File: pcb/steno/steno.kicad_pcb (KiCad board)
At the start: 2 copper layers, 259.5 x 85.1 mm, 61 parts, among them J1 USB_C_Receptacle_USB2.0, K1 PG1350, K10 PG1350, K11 PG1350, K12 PG1350, K13 PG1350, K14 PG1350, K15 PG1350, K16 PG1350, K17 PG1350, K18 PG1350, K19 PG1350, K2 PG1350, K20 PG1350, K21 PG1350, K22 PG1350, K23 PG1350, K24 PG1350, K25 PG1350, K26 PG1350, K27 PG1350, K28 PG1350, K29 PG1350, K3 PG1350, K30 PG1350, K4 PG1350, K5 PG1350, K6 PG1350, K7 PG1350, K8 PG1350, K9 PG1350, SW1 SW_Push, SW2 SW_Push, U1 ATmega32U4-AU, U2 MT25QL128ABA1ESE, U3 MCP1700-3302E_SOT23, U4 LCD2.2in, U5 4050, U6 SRV05-4, Y1 16MHz

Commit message: [pcb] 2 row Auklet
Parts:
- removed C10, C9: 1uF, Capacitor_SMD:C_0805_2012Metric
- removed C5, C6, C7: 104, Capacitor_SMD:C_0603_1608Metric
- removed C8: 10uF, Capacitor_SMD:C_0805_2012Metric
- removed F1: Polyfuse_Small, Fuse:Fuse_1206_3216Metric_Castellated
- removed Y1: 16MHz, Crystal:Crystal_SMD_EuroQuartz_MT-4Pin_3.2x2.5mm
- added BT1: Battery_Cell, Connector_JST:JST_PH_S2B-PH-SM4-TB_1x02-1MP_P2.00mm_Horizontal, F.Cu at (156.6, 67.7)
- added D1: RED, LED_SMD:LED_0805_2012Metric, F.Cu at (146.9, 54.7)
- added D2: LED_RABG, LED_SMD:LED_ASMB-KTF0-0A306, F.Cu at (135.4, 65.5)
- added H1: MountingHole, misc:auklet-mount, F.Cu at (138.9, 100.7)
- added H2: MountingHole, misc:auklet-cover-mount, F.Cu at (138.9, 100.7)
- added J2: USB_C_Receptacle_USB2.0, Connector_USB:USB_C_Receptacle_HRO_TYPE-C-31-M-12, F.Cu at (138.9, 56.9)
- added Q1: AO3401A, Package_TO_SOT_SMD:SOT-23, F.Cu at (144.9, 76.2)
- added R1: 100k, Resistor_SMD:R_0603_1608Metric, F.Cu at (114.4, 78.7)
- added R13: 5.1M, Resistor_SMD:R_0603_1608Metric, F.Cu at (134.4, 69.7)
- added R14: 5.1M, Resistor_SMD:R_0603_1608Metric, F.Cu at (133.6, 67.5)
- added R15: 1.2k, Resistor_SMD:R_0603_1608Metric, F.Cu at (132.1, 59.2)
- added R16: 1.5k, Resistor_SMD:R_0603_1608Metric, F.Cu at (132.1, 65.0)
- added R17: 1k, Resistor_SMD:R_0603_1608Metric, F.Cu at (132.6, 62.7)
- added R6: 220, Resistor_SMD:R_0603_1608Metric, F.Cu at (116.6, 112.2)
- added REF**: crides-neg, misc:crides-neg, F.Cu at (87.4, 102.7)
- added REF**: embedded, misc:embedded, F.Cu at (99.9, 105.2)
- C1, C2: value 22pF -> 4.7uF; moved to F.Cu
- C3: value 1uF -> 4.7uF; footprint Capacitor_SMD:C_0805_2012Metric -> Capacitor_SMD:C_0603_1608Metric; moved to F.Cu
- C4: value 1uF -> 10nF; footprint Capacitor_SMD:C_0805_2012Metric -> Capacitor_SMD:C_0603_1608Metric; moved to F.Cu
- J1: value USB_C_Receptacle_USB2.0 -> Conn_01x04; footprint Connector_USB:USB_C_Receptacle_HRO_TYPE-C-31-M-12 -> keeb-libs:debug-port-single-side
- K1, K10, K11, K12, K13, K14, K15, K16, K17, K18, K19, K2, K20, K21, K22, K23, K24, K25, K26, K27, K28, K29, K3, K30, K4, K5, K6, K7, K8, K9: value PG1350 -> diode-choc; footprint pg1350:PG1350 -> pg1350:pg1350-D
- R10: value 220 -> 10k; moved to F.Cu
- R11: value 5.1k -> 10k; moved to F.Cu
- R12: value 5.1k -> 1k; moved to F.Cu
- R2, R3: value 22 -> 220; moved to F.Cu
- R4: value 10k -> 100; footprint Resistor_SMD:R_0805_2012Metric -> Resistor_SMD:R_0603_1608Metric; moved to F.Cu
- R5: value 10k -> 220; footprint Resistor_SMD:R_0805_2012Metric -> Resistor_SMD:R_0603_1608Metric; moved to F.Cu
- R7: value 220 -> 100k; moved to F.Cu
- R8, R9: value 220 -> 5.1k; moved to F.Cu
- SW1: value SW_Push -> SW_SPDT; footprint Button_Switch_SMD:SW_SPST_B3U-1000P -> Button_Switch_SMD:SW_SPDT_PCM12
- SW2: footprint Button_Switch_SMD:SW_SPST_B3U-1000P -> Button_Switch_SMD:SW_SPST_TL3342
- U1: value ATmega32U4-AU -> MT25QL128ABA1ESE; footprint Package_QFP:TQFP-44_10x10mm_P0.8mm -> Package_SO:SOP-8_5.28x5.23mm_P1.27mm; moved to F.Cu
- U2: value MT25QL128ABA1ESE -> LCD2.2in; footprint Package_SO:SOP-8_5.28x5.23mm_P1.27mm -> misc:TM022HDH26; moved to F.Cu
- U3: value MCP1700-3302E_SOT23 -> Holyiot_18010_no_underside; footprint Package_TO_SOT_SMD:SOT-23 -> keeb-libs:Holyiot-18010-no-underside; moved to F.Cu
- U4: value LCD2.2in -> BQ24075; footprint steno:LCD2.2in -> Package_DFN_QFN:VQFN-16-1EP_3x3mm_P0.5mm_EP1.68x1.68mm_ThermalVias
- U5: value 4050 -> XC6206B331MR; footprint Package_SO:SOIC-16_3.9x9.9mm_P1.27mm -> Package_TO_SOT_SMD:SOT-23-5; moved to F.Cu
- U6: moved to F.Cu
- moved R9 52.9 mm to (132.1, 57.7)
- moved R8 52.0 mm to (145.1, 57.2), turned to -90 degrees
- moved R3 45.8 mm to (116.6, 109.2), turned to 180 degrees
- moved R2 45.2 mm to (116.6, 107.7), turned to 180 degrees
- moved R7 37.6 mm to (146.9, 73.0), turned to 90 degrees
- moved U5 36.4 mm to (148.6, 67.2)
- moved R10 35.7 mm to (143.1, 71.0), turned to -90 degrees
- moved J1 31.8 mm to (108.6, 56.7), turned to 15 degrees
- moved R5 25.7 mm to (116.6, 110.7), turned to 180 degrees
- moved U4 25.5 mm to (144.6, 67.2), turned to 90 degrees
- moved U1 24.9 mm to (118.4, 75.0), turned to 180 degrees
- moved C1 21.7 mm to (142.4, 64.0)
- moved U3 20.2 mm to (122.9, 61.9)
- moved R4 17.2 mm to (144.6, 73.7)
- moved SW2 16.0 mm to (133.6, 74.2), turned to 0 degrees
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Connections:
- C1 pad 1: Net-(C1-Pad1) -> VBUS
- C2 pad 1: Net-(C2-Pad1) -> GND
- C2 pad 2: GND -> /power/VDDH
- C3 pad 1: GND -> /power/BAT
- C3 pad 2: Net-(C3-Pad2) -> GND
- C4 pad 1: Net-(C4-Pad1) -> BAT_MEAS
- K1 pad 1: ROW1 -> R1
- K1 pad 2: COL1 -> C1
- K1 pad 3: Net-(K1-Pad3) -> (no net)
- K10 pad 1: ROW2 -> R2
- K10 pad 2: COL4 -> C4
- K10 pad 3: Net-(K10-Pad3) -> (no net)
- K11 pad 1: ROW2 -> R2
- K11 pad 2: COL5 -> C5
- K11 pad 3: Net-(K11-Pad3) -> (no net)
- K12 pad 1: ROW2 -> R2
- K12 pad 2: COL6 -> C6
- K12 pad 3: Net-(K12-Pad3) -> (no net)
- K13 pad 1: ROW3 -> R3
- K13 pad 2: COL1 -> C1
- K13 pad 3: Net-(K13-Pad3) -> (no net)
- K14 pad 1: ROW3 -> R3
- K14 pad 2: COL2 -> C2
- K14 pad 3: Net-(K14-Pad3) -> (no net)
- K15 pad 1: ROW3 -> R3
- K15 pad 2: COL3 -> C3
- K15 pad 3: Net-(K15-Pad3) -> (no net)
- K16 pad 1: ROW3 -> R3
- K16 pad 2: COL4 -> C4
- K16 pad 3: Net-(K16-Pad3) -> (no net)
- K17 pad 1: ROW3 -> R3
- K17 pad 2: COL5 -> C5
- K17 pad 3: Net-(K17-Pad3) -> (no net)
- K18 pad 1: ROW3 -> R3
- K18 pad 2: COL6 -> C6
- K18 pad 3: Net-(K18-Pad3) -> (no net)
- K19 pad 1: ROW4 -> R4
- K19 pad 2: COL1 -> C1
- K19 pad 3: Net-(K19-Pad3) -> (no net)
- K2 pad 1: ROW1 -> R1
- K2 pad 2: COL2 -> C2
- K2 pad 3: Net-(K2-Pad3) -> (no net)
- K20 pad 1: ROW4 -> R4
- K20 pad 2: COL2 -> C2
- K20 pad 3: Net-(K20-Pad3) -> (no net)
- K21 pad 1: ROW4 -> R4
- K21 pad 2: COL3 -> C3
- K21 pad 3: Net-(K21-Pad3) -> (no net)
- K22 pad 1: ROW4 -> R4
- K22 pad 2: COL4 -> C4
- K22 pad 3: Net-(K22-Pad3) -> (no net)
- K23 pad 1: ROW4 -> R4
- K23 pad 2: COL5 -> C5
- K23 pad 3: Net-(K23-Pad3) -> (no net)
- K24 pad 1: ROW4 -> R4
- K24 pad 2: COL6 -> C6
- K24 pad 3: Net-(K24-Pad3) -> (no net)
- K25 pad 1: ROW5 -> R5
- K25 pad 2: COL1 -> C1
- K25 pad 3: Net-(K25-Pad3) -> (no net)
- K26 pad 1: ROW5 -> R5
- K26 pad 2: COL2 -> C2
- K26 pad 3: Net-(K26-Pad3) -> (no net)
- K27 pad 1: ROW5 -> R5
- K27 pad 2: COL3 -> C3
- K27 pad 3: Net-(K27-Pad3) -> (no net)
- K28 pad 1: ROW5 -> R5
- K28 pad 2: COL4 -> C4
- K28 pad 3: Net-(K28-Pad3) -> (no net)
- K29 pad 1: ROW5 -> R5
- K29 pad 2: COL5 -> C5
- K29 pad 3: Net-(K29-Pad3) -> (no net)
- K3 pad 1: ROW1 -> R1
- K3 pad 2: COL3 -> C3
- K3 pad 3: Net-(K3-Pad3) -> (no net)
- K30 pad 1: ROW5 -> R5
- K30 pad 2: COL6 -> C6
- K30 pad 3: Net-(K30-Pad3) -> (no net)
- K4 pad 1: ROW1 -> R1
- K4 pad 2: COL4 -> C4
- K4 pad 3: Net-(K4-Pad3) -> (no net)
- K5 pad 1: ROW1 -> R1
- K5 pad 2: COL5 -> C5
- K5 pad 3: Net-(K5-Pad3) -> (no net)
- K6 pad 1: ROW1 -> R1
- K6 pad 2: COL6 -> C6
- K6 pad 3: Net-(K6-Pad3) -> (no net)
- K7 pad 1: ROW2 -> R2
- K7 pad 2: COL1 -> C1
- K7 pad 3: Net-(K7-Pad3) -> (no net)
- K8 pad 1: ROW2 -> R2
- K8 pad 2: COL2 -> C2
- K8 pad 3: Net-(K8-Pad3) -> (no net)
- K9 pad 1: ROW2 -> R2
- K9 pad 2: COL3 -> C3
- K9 pad 3: Net-(K9-Pad3) -> (no net)
- R11 pad 1: GND -> Net-(R11-Pad1)
- R11 pad 2: Net-(J1-PadA5) -> GND
- R12 pad 1: GND -> Net-(R12-Pad1)
- R12 pad 2: Net-(J1-PadB5) -> Net-(D1-Pad1)
- R2 pad 2: D+ -> GND
- R3 pad 2: D- -> GND
- R4 pad 1: GND -> BL
- R4 pad 2: Net-(R4-Pad2) -> Net-(Q1-Pad1)
- R5 pad 2: +3V3 -> GND
- R7 pad 1: Net-(R7-Pad1) -> Net-(Q1-Pad1)
- R8 pad 1: Net-(R8-Pad1) -> GND
- R8 pad 2: GND -> Net-(J2-PadA5)
- R9 pad 1: Net-(R9-Pad1) -> GND
- R9 pad 2: GND -> Net-(J2-PadB5)
- SW1 pad 1: GND -> VBUS
- SW1 pad 2: RESET -> Net-(SW1-Pad2)
- U1 pad 1: Net-(U1-Pad1) -> FLASH_CS
- U1 pad 2: +5V -> MISO
- U1 pad 3: Net-(R3-Pad1) -> DQ2
- U1 pad 4: Net-(R2-Pad1) -> GND
- U1 pad 5: GND -> MOSI
- U1 pad 6: Net-(C4-Pad1) -> SCLK
- U1 pad 7: +5V -> DQ2
- U1 pad 8: Net-(SW2-Pad2) -> +3V3
- U2 pad 1: CS_3V3 -> GND
- U2 pad 2: MISO -> +3V3
- U2 pad 3: Net-(R5-Pad1) -> SCLK
- U2 pad 4: GND -> C\D
- U2 pad 5: MOSI_3V3 -> LCD_CS
- U2 pad 6: SCLK_3V3 -> MOSI
- U2 pad 7: Net-(R5-Pad1) -> MISO
- U2 pad 8: +3V3 -> GND
- U3 pad 2: +3V3 -> unconnected-(U3-Pad2)
- U3 pad 3: +5V -> unconnected-(U3-Pad3)
- U4 pad 1: GND -> Net-(R10-Pad1)
- U4 pad 10: +3V3 -> /power/VDDH
- U4 pad 11: Net-(R7-Pad1) -> /power/VDDH
- U4 pad 12: Net-(R8-Pad1) -> unconnected-(U4-Pad12)
- U4 pad 13: Net-(R9-Pad1) -> VBUS
- U4 pad 14: Net-(R10-Pad1) -> unconnected-(U4-Pad14)
- U4 pad 2: +3V3 -> /power/BAT
- U4 pad 3: SCLK_3V3 -> /power/BAT
- U4 pad 4: C\D_3V3 -> GND
- U4 pad 5: LCD_CS_3V3 -> GND
- U4 pad 6: MOSI_3V3 -> /power/VDDH
- U4 pad 7: MISO -> unconnected-(U4-Pad7)
- U4 pad 9: +3V3 -> Net-(R12-Pad1)
- U5 pad 1: +3V3 -> /power/VDDH
- U5 pad 2: SCLK_3V3 -> GND
- U5 pad 3: SCLK_5V -> Net-(SW1-Pad2)
- U5 pad 4: MOSI_3V3 -> unconnected-(U5-Pad4)
- U5 pad 5: MOSI_5V -> +3V3
- U6 pad 1: Net-(U6-Pad1) -> D+
- U6 pad 3: Net-(U6-Pad3) -> D-
- U6 pad 4: D+ -> D-
- U6 pad 5: VCC -> VBUS
- U6 pad 6: D- -> D+
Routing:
- net C1: track 0.00 -> 358.0 mm, vias 0 -> 3
- net COL1: track 329.7 -> 0.00 mm, vias 1 -> 0
- net C2: track 0.00 -> 322.3 mm, vias 0 -> 5
- net COL2: track 292.9 -> 0.00 mm, vias 3 -> 0
- net C3: track 0.00 -> 290.5 mm, vias 0 -> 5
- net COL3: track 260.4 -> 0.00 mm, vias 3 -> 0
- net C4: track 0.00 -> 256.3 mm, vias 0 -> 5
- net COL4: track 224.5 -> 0.00 mm, vias 3 -> 0
- net C5: track 0.00 -> 218.3 mm, vias 0 -> 5
- net R3: track 0.00 -> 190.4 mm, vias 0 -> 2
- net COL5: track 184.8 -> 0.00 mm, vias 3 -> 0
- net C6: track 0.00 -> 178.0 mm, vias 0 -> 5
- net ROW3: track 161.7 -> 0.00 mm
- net COL6: track 148.9 -> 0.00 mm, vias 3 -> 0
- net R5: track 0.00 -> 146.2 mm, vias 0 -> 1
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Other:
- board size 259.5 x 85.1 mm -> 268.1 x 85.4 mm
- net class Default removed
- board text added: "Auklet (embedded steno board v4) Open sourced @ github.com/crides/steno"
- board text added: "No"
- board text added: "Use Bat"
- board text added: "Yes"
- board text removed: "BatWings Embedded steno gives you wings!"
- board text removed: "Open sourced @ github.com/crides/steno"
- board text removed: "Public test #1"

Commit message: [pcb] Auklet 3
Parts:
- added K32: diode-choc, pg1350:pg1350-D, F.Cu at (36.2, 103.5)
- added K33: diode-choc, pg1350:pg1350-D, F.Cu at (54.8, 101.7)
- added K34: diode-choc, pg1350:pg1350-D, F.Cu at (73.1, 101.9)
- added K35: diode-choc, pg1350:pg1350-D, F.Cu at (90.3, 108.0)
- added K36: diode-choc, pg1350:pg1350-D, F.Cu at (108.0, 111.1)
- added K38: diode-choc, pg1350:pg1350-D, F.Cu at (259.3, 103.5)
- added K39: diode-choc, pg1350:pg1350-D, F.Cu at (240.7, 101.7)
- added K40: diode-choc, pg1350:pg1350-D, F.Cu at (222.5, 101.9)
- added K41: diode-choc, pg1350:pg1350-D, F.Cu at (205.3, 108.0)
- added K42: diode-choc, pg1350:pg1350-D, F.Cu at (187.6, 111.1)
- moved BT1 114.9 mm to (269.1, 91.1)
- moved REF** 35.3 mm to (65.5, 113.2)
- moved REF** 35.0 mm to (53.3, 110.6)
- moved K30 8.96 mm to (184.6, 94.3)
- moved C3 8.96 mm to (154.5, 69.3)
- moved R13 8.96 mm to (143.3, 68.8)
- moved U5 8.96 mm to (157.5, 66.3)
- moved C1 8.96 mm to (151.3, 63.0)
- moved K8 8.96 mm to (39.2, 86.8)
- moved U2 8.96 mm to (147.8, 104.8)
- moved K14 8.96 mm to (100.6, 127.5)
- moved R9 8.96 mm to (141.0, 56.8)
- moved U6 8.96 mm to (147.8, 64.0)
- moved K4 8.96 mm to (79.0, 68.4)
- moved K9 8.96 mm to (57.8, 85.0)
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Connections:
- K13 pad 1: R3 -> R4
- K14 pad 1: R3 -> R4
- K15 pad 1: R3 -> R4
- K16 pad 1: R3 -> R4
- K17 pad 1: R3 -> R4
- K18 pad 1: R3 -> R4
- K19 pad 1: R4 -> R5
- K20 pad 1: R4 -> R5
- K21 pad 1: R4 -> R5
- K22 pad 1: R4 -> R5
- K23 pad 1: R4 -> R5
- K24 pad 1: R4 -> R5
- K25 pad 1: R5 -> R6
- K26 pad 1: R5 -> R6
- K27 pad 1: R5 -> R6
- K28 pad 1: R5 -> R6
- K29 pad 1: R5 -> R6
- K30 pad 1: R5 -> R6
- U3 pad 41: R4 -> R5
- U3 pad 42: R5 -> R6
- U3 pad 43: R3 -> R4
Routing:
- net R6: track 0.00 -> 146.2 mm, vias 0 -> 1
- net /power/BAT: track 28.2 -> 147.9 mm, vias 3 -> 5
- net R3: track 190.4 -> 76.6 mm, vias 2 -> 0
- net GND: track 131.2 -> 231.2 mm, vias 18 -> 19
- net R7: track 0.00 -> 76.6 mm
- net C3: track 290.5 -> 341.9 mm
- net R4: track 140.0 -> 189.1 mm, vias 1 -> 2
- net C2: track 322.3 -> 371.2 mm
- net C5: track 218.3 -> 266.3 mm
- net C4: track 256.3 -> 304.0 mm
- net C6: track 178.0 -> 213.7 mm
- net C1: track 358.0 -> 393.3 mm
- net R5: track 146.2 -> 140.0 mm
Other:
- board size 268.1 x 85.4 mm -> 268.7 x 85.3 mm
- board text added: "+ -"

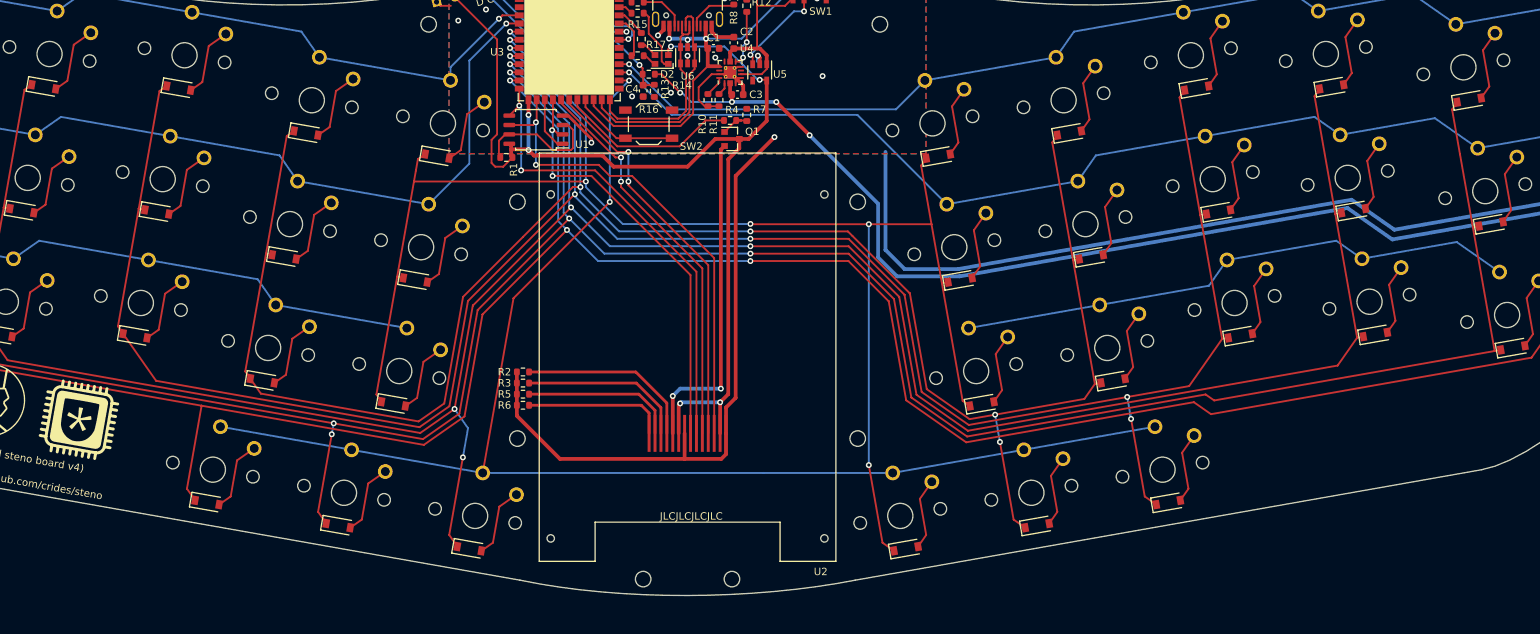
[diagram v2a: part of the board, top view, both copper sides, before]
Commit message: [pcb] auklet 3: use new libraries
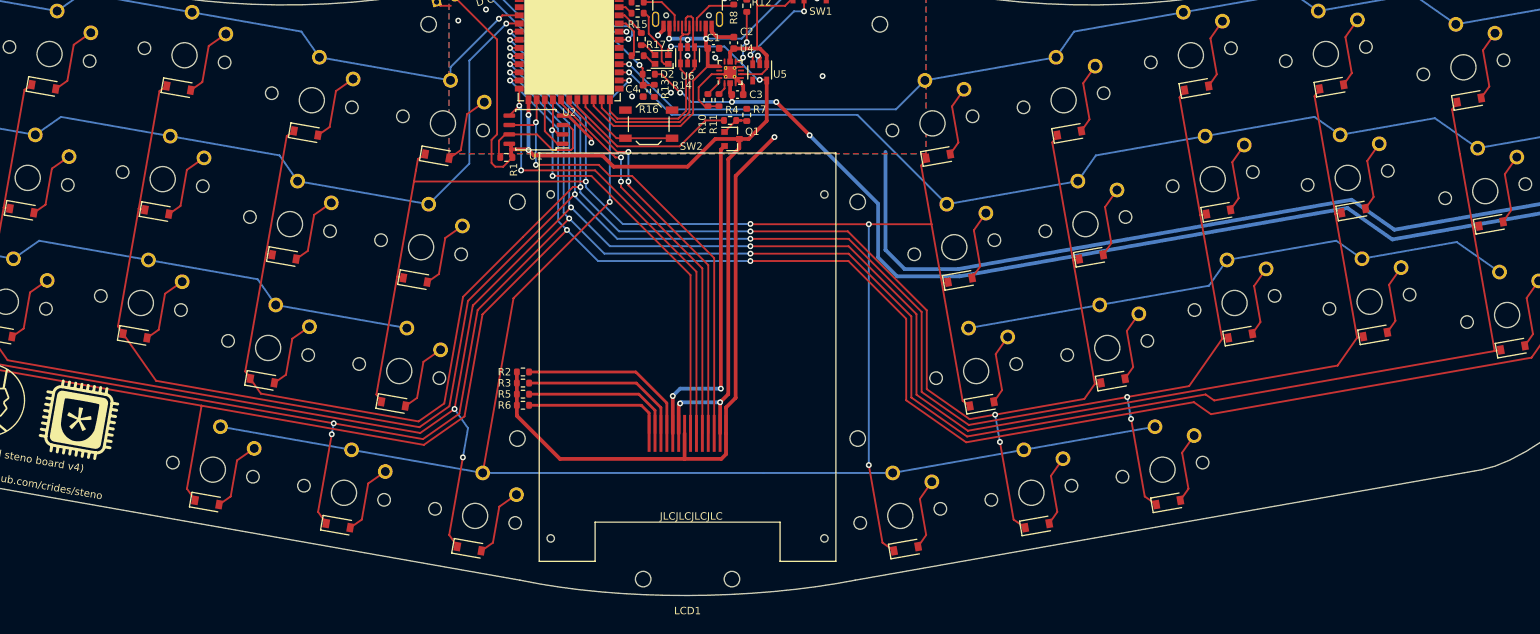
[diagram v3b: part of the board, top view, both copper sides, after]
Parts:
- LCD1: renamed from U2; value LCD2.2in -> TM022HDH26; footprint misc:TM022HDH26 -> display:TM022HDH26
- U1: footprint Package_SO:SOP-8_5.28x5.23mm_P1.27mm -> Package_SO:SOIC-8_5.23x5.23mm_P1.27mm
- U2: renamed from U3; value Holyiot_18010_no_underside -> holyiot-18010-no-underside; footprint keeb-libs:Holyiot-18010-no-underside -> mcu:Holyiot-18010-no-underside
- renumbered K32 to K31, K33 to K32, K34 to K33, K35 to K34, K36 to K35, K38 to K36, K39 to K37, K40 to K38, K41 to K39, K42 to K40
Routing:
- net C1: track 393.3 -> 394.0 mm
- net C3: track 341.9 -> 342.7 mm
- net C2: track 371.2 -> 371.9 mm
- net C4: track 304.0 -> 304.8 mm
- net C5: track 266.3 -> 267.1 mm

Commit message: [pcb] Auklet 3: first revision
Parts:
- J1: value Conn_01x04 -> debug-port; footprint keeb-libs:debug-port-single-side -> misc:debug-port-single-side
- U2: footprint mcu:Holyiot-18010-no-underside -> mcu:holyiot-18010-no-underside
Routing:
- net GND: track 231.2 -> 228.4 mm, vias 19 -> 20
- net Net-(SW1-Pad2): track 12.9 -> 11.3 mm
- net DQ2: track 17.8 -> 17.0 mm
- net Net-(Q1-Pad1): track 4.24 -> 3.57 mm
- net MISO: track 57.4 -> 56.8 mm

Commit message: [pcb] Auklet: add tooling holes
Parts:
- added REF**: jlc-tooling-hole, misc:jlc-tooling-hole, F.Cu at (147.8, 131.0)
- added REF**: jlc-tooling-hole, misc:jlc-tooling-hole, F.Cu at (21.8, 55.3)
- added REF**: jlc-tooling-hole, misc:jlc-tooling-hole, F.Cu at (272.8, 55.3)
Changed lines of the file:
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@@
     )
+  )
+  (footprint "misc:jlc-tooling-hole" (layer "F.Cu")
+    (at 147.775972 131.027909)
+    (attr through_hole board_only exclude_from_pos_files exclude_from_bom)
+    (fp_text reference "REF**" (at 0 -4 unlocked) (layer "F.SilkS") hide
+      (effects (font (size 1 1) (thickness 0.15)))
+    )
+    (fp_text value "jlc-tooling-hole" (at 0 1.5 unlocked) (layer "F.Fab")
+      (effects (font (size 1 1) (thickness 0.15)))
+    )
+    (pad "" np_thru_hole circle (at 0 0) (size 1.3 1.3) (drill 1.152) (layers *.Mask))
   )
   (footprint "misc:auklet-mount" (layer "F.Cu")
@@
     )
   )
+  (footprint "misc:jlc-tooling-hole" (layer "F.Cu")
+    (at 21.775972 55.277909)
+    (attr through_hole board_only exclude_from_pos_files exclude_from_bom)
+    (fp_text reference "REF**" (at 0 -4 unlocked) (layer "F.SilkS") hide
+      (effects (font (size 1 1) (thickness 0.15)))
+    )
+    (fp_text value "jlc-tooling-hole" (at 0 1.5 unlocked) (layer "F.Fab")
+      (effects (font (size 1 1) (thickness 0.15)))
+    )
+    (pad "" np_thru_hole circle (at 0 0) (size 1.3 1.3) (drill 1.152) (layers *.Mask))
+  )
   (footprint "misc:embedded" (layer "F.Cu")
     (at 65.503681 113.236795 -10)
@@
     )
   )
+  (footprint "misc:jlc-tooling-hole" (layer "F.Cu")
+    (at 272.775972 55.277909)
+    (attr through_hole board_only exclude_from_pos_files exclude_from_bom)
+    (fp_text reference "REF**" (at 0 -4 unlocked) (layer "F.SilkS") hide
+      (effects (font (size 1 1) (thickness 0.15)))
+    )
+    (fp_text value "jlc-tooling-hole" (at 0 1.5 unlocked) (layer "F.Fab")
+      (effects (font (size 1 1) (thickness 0.15)))
+    )
+    (pad "" np_thru_hole circle (at 0 0) (size 1.3 1.3) (drill 1.152) (layers *.Mask))
+  )
   (footprint "Resistor_SMD:R_0603_1608Metric" (layer "F.Cu")

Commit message: fix(auklet): display pin order, routing
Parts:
- removed H1: MountingHole, misc:auklet-mount
- J1: value debug-port -> jlink; footprint misc:debug-port-single-side -> Connector_PinHeader_1.27mm:PinHeader_2x05_P1.27mm_Vertical_SMD
- LCD1: footprint display:TM022HDH26 -> display:TM022HDH26_back
- moved R5 47.1 mm to (172.5, 105.5), turned to 0 degrees
- moved R3 47.1 mm to (172.5, 104.0), turned to 0 degrees
- moved R2 47.1 mm to (172.5, 102.5), turned to 0 degrees
- moved R6 47.1 mm to (172.5, 107.0), turned to 0 degrees
- moved REF** 27.5 mm to (175.2, 128.8)
- moved SW2 27.2 mm to (167.5, 62.5)
- moved U1 15.0 mm to (127.7, 89.0), turned to 90 degrees
- moved Q1 10.8 mm to (161.2, 67.5), turned to 90 degrees
- moved R1 6.46 mm to (126.2, 83.5), turned to 180 degrees
- moved LCD1 5.60 mm to (150.7, 100.0)
- moved R9 5.29 mm to (144.5, 52.8), turned to -90 degrees
- moved R7 4.97 mm to (158.7, 68.0)
- moved R16 4.78 mm to (144.0, 60.3)
- moved K5 4.58 mm to (99.2, 71.0)
- moved REF** 4.58 mm to (24.7, 51.8)
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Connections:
- J1 pad 1: GND -> +3V3
- J1 pad 2: +3V3 -> SWD
- J1 pad 3: SWD -> GND
- SW2 pad 2: Net-(SW2-Pad2) -> ~{RST}
- U2 pad 13: MOSI -> FLASH_CS
- U2 pad 3: unconnected-(U2-Pad3) -> R1
- U2 pad 4: R1 -> R2
- U2 pad 40: unconnected-(U2-Pad40) -> R5
- U2 pad 41: R5 -> R6
- U2 pad 42: R6 -> R7
- U2 pad 48: Net-(SW2-Pad2) -> ~{RST}
- U2 pad 5: R2 -> R3
- U2 pad 50: C\D -> LCD_CS
- U2 pad 51: LCD_CS -> C\D
- U2 pad 53: FLASH_CS -> MOSI
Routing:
- net ~{RST}: track 0.00 -> 66.7 mm, vias 0 -> 4
- net R7: track 76.6 -> 138.0 mm, vias 0 -> 1
- net R3: track 76.6 -> 123.0 mm, vias 0 -> 1
- net FLASH_CS: track 7.37 -> 29.7 mm
- net Net-(SW2-Pad2): track 14.4 -> 0.00 mm
- net MISO: track 56.8 -> 70.8 mm, vias 2 -> 3
- net C6: track 213.7 -> 227.7 mm, vias 5 -> 4
- net GND: track 228.4 -> 242.1 mm, vias 20 -> 22
- net DQ2: track 17.0 -> 9.45 mm
- net +3V3: track 147.5 -> 140.1 mm, vias 6 -> 8
- net C3: track 342.7 -> 349.7 mm, vias 5 -> 3
- net /power/BAT: track 147.9 -> 140.9 mm
- net C5: track 267.1 -> 260.2 mm, vias 5 -> 4
- net C4: track 304.7 -> 298.0 mm, vias 5 -> 4
- net R4: track 189.1 -> 183.3 mm, vias 2 -> 1
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
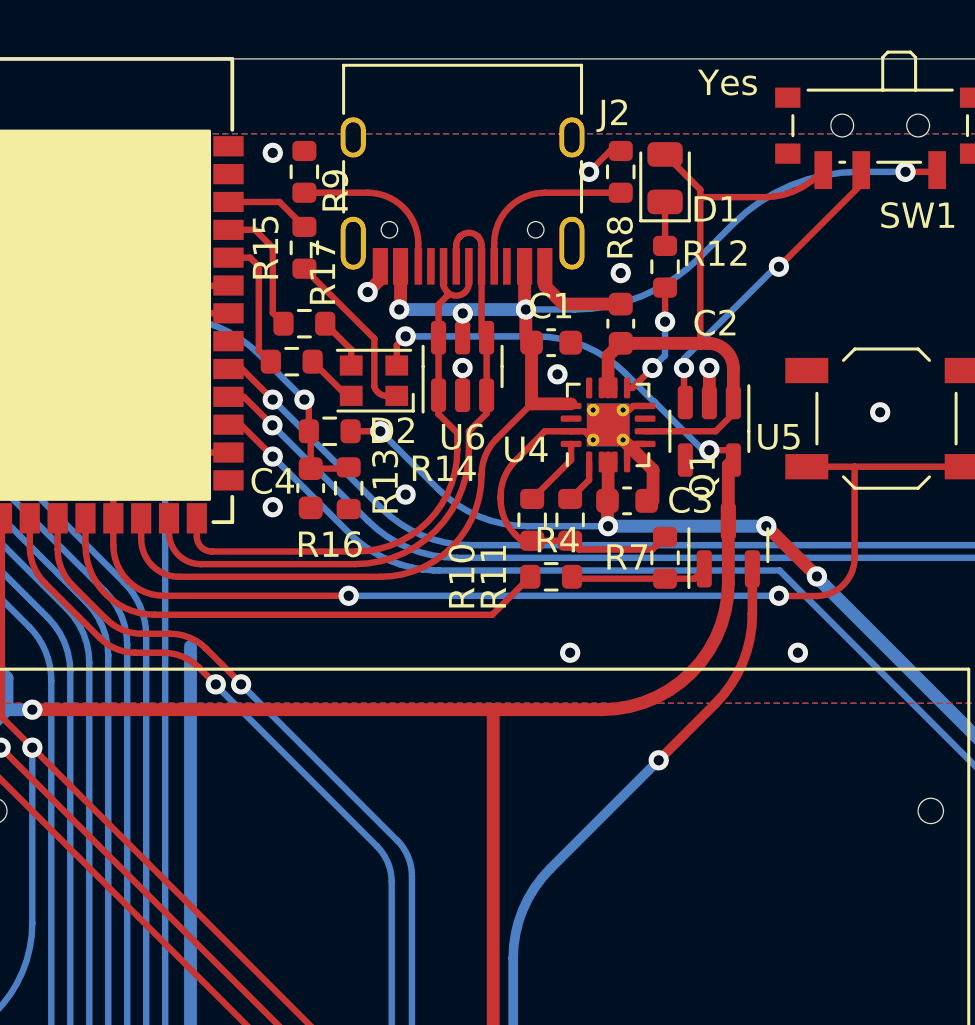
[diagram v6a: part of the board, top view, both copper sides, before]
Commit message: fix(auklet): backlight MOSFET
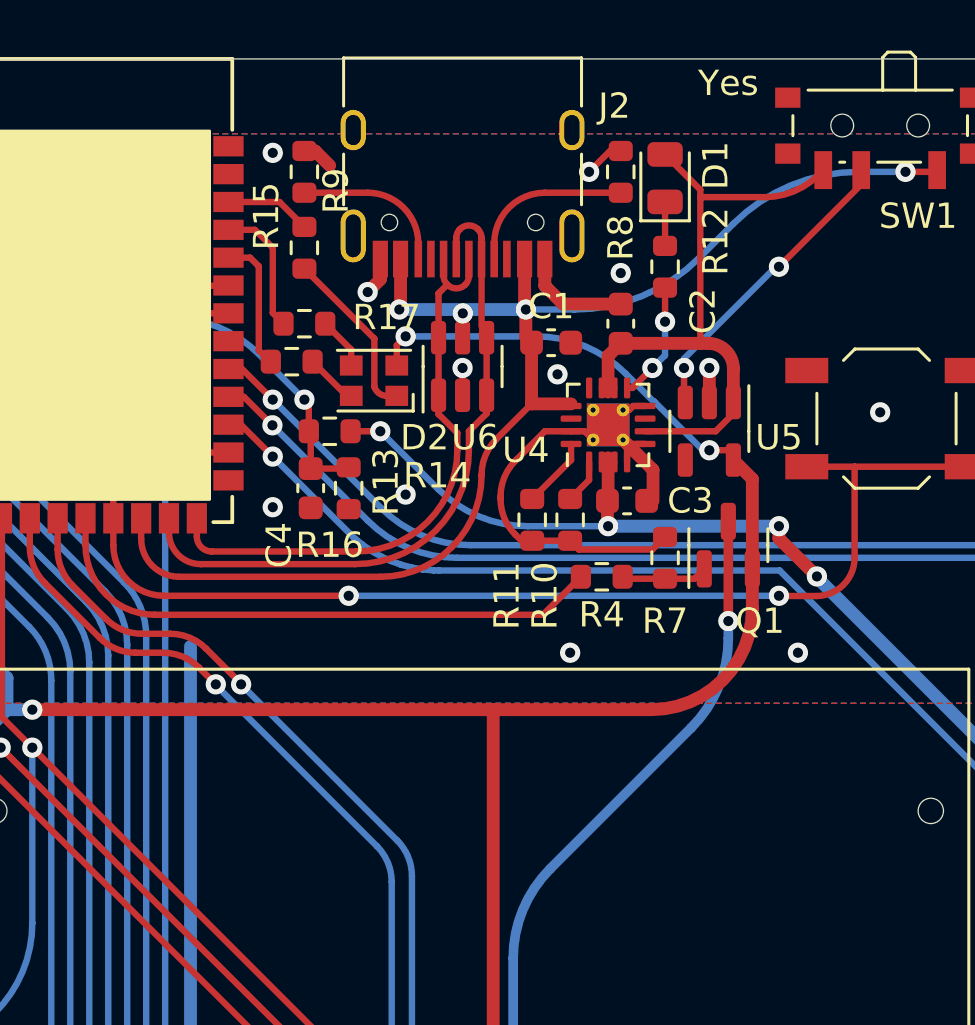
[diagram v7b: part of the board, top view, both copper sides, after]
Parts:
- moved R4 2.00 mm to (156.2, 68.8)
- moved J2 0.29 mm to (150.7, 52.2)
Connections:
- Q1 pad 2: Net-(LCD1-Pad10) -> +3V3
- Q1 pad 3: +3V3 -> Net-(LCD1-Pad10)
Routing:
- net BL: track 20.7 -> 22.7 mm
- net Net-(Q1-Pad1): track 5.42 -> 3.42 mm
- net +3V3: track 140.1 -> 141.7 mm
- net Net-(LCD1-Pad10): track 44.7 -> 46.2 mm
- net GND: track 242.1 -> 243.4 mm
